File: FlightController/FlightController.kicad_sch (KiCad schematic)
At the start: 30 parts, among them J1 FTSH-107-01-L-DV-K-A, J3 M55-7104042R, J5 Conn_01x02_Pin, SW1 SW_TL1015AF160QG, SW2 SW_TL1015AF160QG, U1 STM32L496RGT6TR, U5 BNO086, U9 TCAN332DCNR, Y2 XTAL_ABS07-32.768KHZ-T

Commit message: Updates to FC
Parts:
- removed J1: FTSH-107-01-L-DV-K-A, inspirefly:SAMTEC_FTSH-107-01-L-DV-K-A, symbol inspirefly:FTSH-107-01-L-DV-K-A
- added C8: 100nF, Capacitor_SMD:C_0402_1005Metric_Pad0.74x0.62mm_HandSolder, symbol Device:C
- added C9: 47uF, Capacitor_SMD:C_1206_3216Metric_Pad1.33x1.80mm_HandSolder, symbol Device:C
- added IC1: MX25L25645GM2I-08G-TR, Package_SO:SOIC-8_5.3x5.3mm_P1.27mm, symbol inspirefly:MX25L25645GM2I-08G-TR
- C1, C18, C2, C22, C24, C25, C26, C27, C28, C3, C33, C4, C5, C6, C7: footprint Capacitor_SMD:C_0402_1005Metric -> Capacitor_SMD:C_0402_1005Metric_Pad0.74x0.62mm_HandSolder
- R10, R2, R22, R25, R7: footprint Resistor_SMD:R_0402_1005Metric -> Resistor_SMD:R_0402_1005Metric_Pad0.72x0.64mm_HandSolder
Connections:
- net +3.3V: now also C8.1, C9.1, IC1.3 (WP#/SIO2), IC1.7 (RESET#/SIO3), IC1.8 (VCC)
- net GND: now also C8.2, C9.2, IC1.4 (GND)
- net SPI3_MISO: now also IC1.2 (SO/SIO1)
- net SPI3_MOSI: now also IC1.5 (SI/SIO0)
- net SPI3_NSS: now also IC1.1 (CS#)
- net SPI3_SCK: now also IC1.6 (SCLK)
- no-connect marks 23 -> 20
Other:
- note added: "NOR Flash"
- moved on the sheet: C18, C24, C25, C26, C27, C28, C6, C7, U1B

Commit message: Board sizes for FC and routing. slight Backplane changes
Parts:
- removed C25: 10nF, Capacitor_SMD:C_0402_1005Metric_Pad0.74x0.62mm_HandSolder, symbol Device:C
- added C10, C11: 22pF, Capacitor_SMD:C_0402_1005Metric_Pad0.74x0.62mm_HandSolder, symbol Device:C_Small
- added H5, H6: MountingHole_Pad, inspirefly:MountingHole_2mm_custom, symbol Mechanical:MountingHole_Pad
- added Y3: XTAL_ABS07-32.768KHZ-T, inspirefly:XTAL_ABS07-32.768KHZ-T, symbol Device:Crystal
- RN1: DESCRIPTION 22k Ohm ±5% 62.5mW Power Per Element Bussed Resistor Networ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 -> (none)
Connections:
- net HEATER_ENABLE is gone; now on net IMU_BOOTN: U1.39 (PC8)
- net FOOTSWITCH: now also U1.37 (PC6)
- net GND: now also C10.1, C11.1, H5.1, H6.1; no longer J3.A17, U5.26 (XOUT32/CLKSEL1)
- net IMU_BOOTN: no longer U1.27 (PB1)
- net at U5.27 (XIN32): now also C11.2, Y3.1
- net EXTERNAL_BAT_CUTOFF renamed SUPER_CAP_CHARGE
- net SUPER_CAP_CHARGE: now also J3.A17
- new net: C10.2, U5.26 (XOUT32/CLKSEL1), Y3.2
- no-connect marks 20 -> 19
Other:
- moved on the sheet: C28

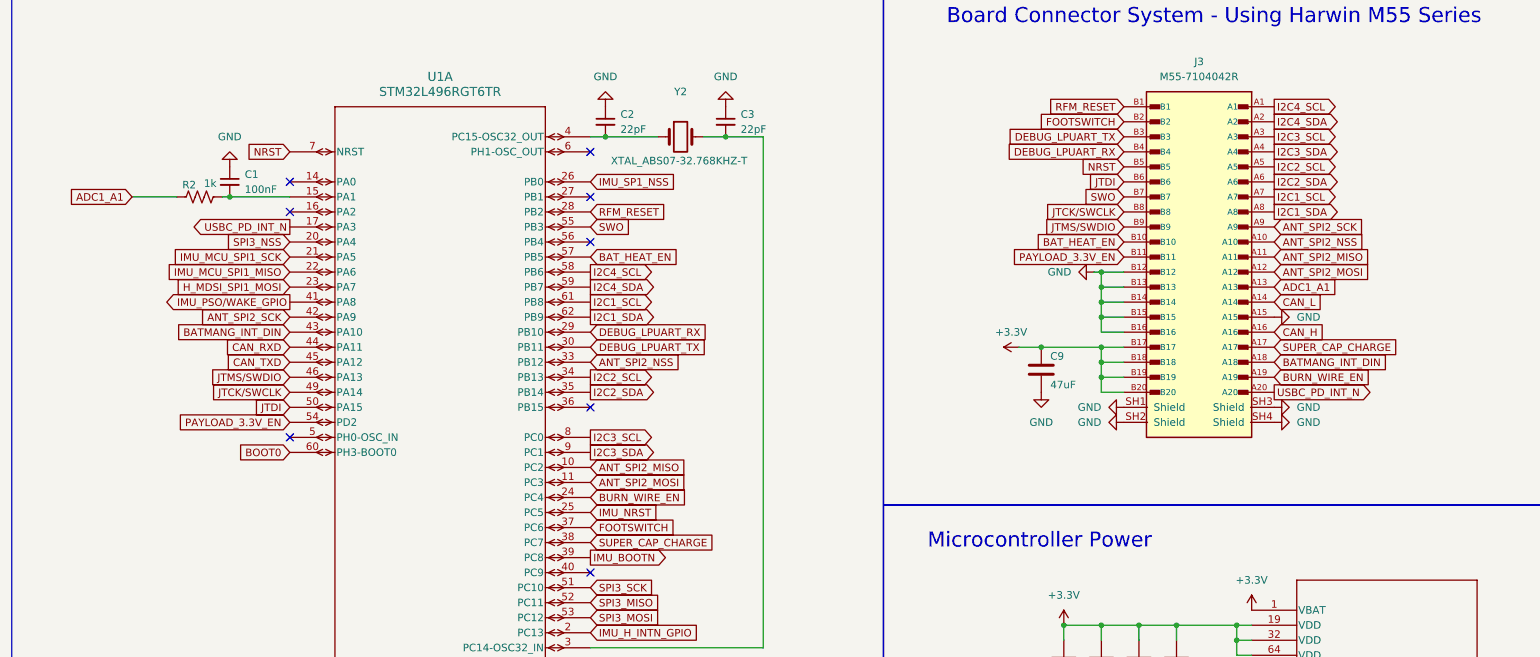
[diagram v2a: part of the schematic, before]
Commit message: Routing and schematic work on most boards
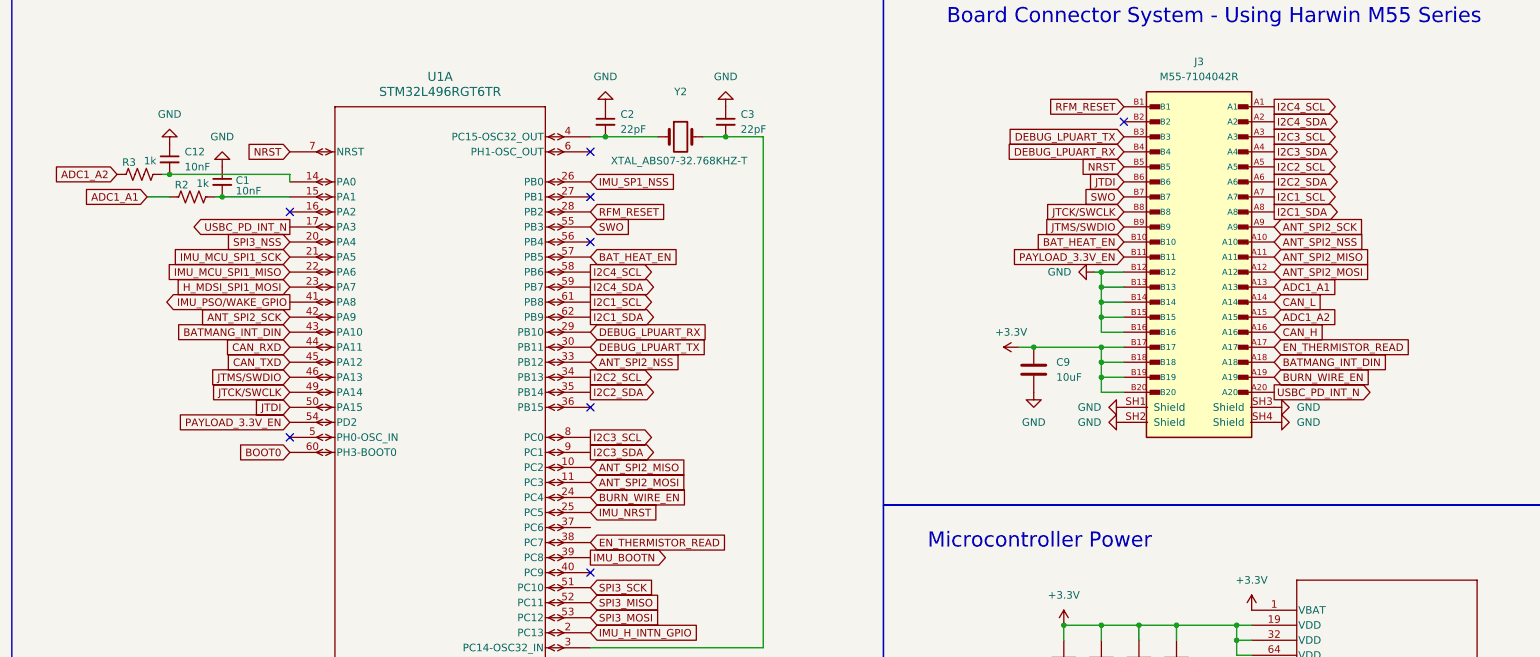
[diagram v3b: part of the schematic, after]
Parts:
- added C12: 10nF, Capacitor_SMD:C_0402_1005Metric_Pad0.74x0.62mm_HandSolder, symbol Device:C_Small
- added R3: 1k, Resistor_SMD:R_0402_1005Metric_Pad0.72x0.64mm_HandSolder, symbol Device:R_US
- C1: value 100nF -> 10nF
- C9: value 47uF -> 10uF; footprint Capacitor_SMD:C_1206_3216Metric_Pad1.33x1.80mm_HandSolder -> Capacitor_SMD:C_0603_1608Metric
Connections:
- net GND: now also C12.1; no longer J3.A15
- net at U1.14 (PA0): now also C12.2, R3.2
- net FOOTSWITCH: no longer names the net of J3.B2
- net FOOTSWITCH: no longer U1.37 (PC6)
- net SUPER_CAP_CHARGE renamed EN_THERMISTOR_READ
- new net ADC1_A2: J3.A15, R3.1
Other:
- moved on the sheet: C1, R2

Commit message: Finalize board work + BOM work
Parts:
- C6: footprint Capacitor_SMD:C_0402_1005Metric_Pad0.74x0.62mm_HandSolder -> Capacitor_SMD:C_0603_1608Metric
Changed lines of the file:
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@@
 			)
 		)
-		(property "Footprint" "Capacitor_SMD:C_0402_1005Metric_Pad0.74x0.62mm_HandSolder"
+		(property "Footprint" "Capacitor_SMD:C_0603_1608Metric"
 			(at 188.9252 179.07 0)
 			(hide yes)
